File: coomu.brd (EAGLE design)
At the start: 25 x 12.1 mm, 23 parts

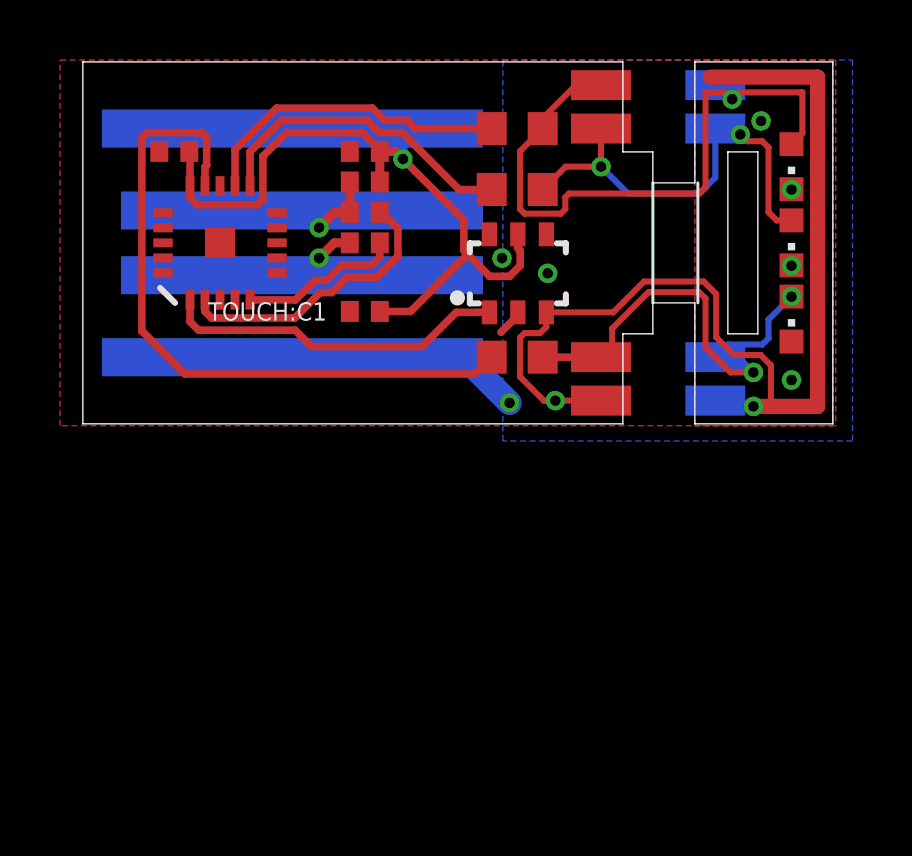
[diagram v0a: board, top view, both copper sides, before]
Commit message: Bob pointed out that LEDs that fire sideways exist. So much simpler.
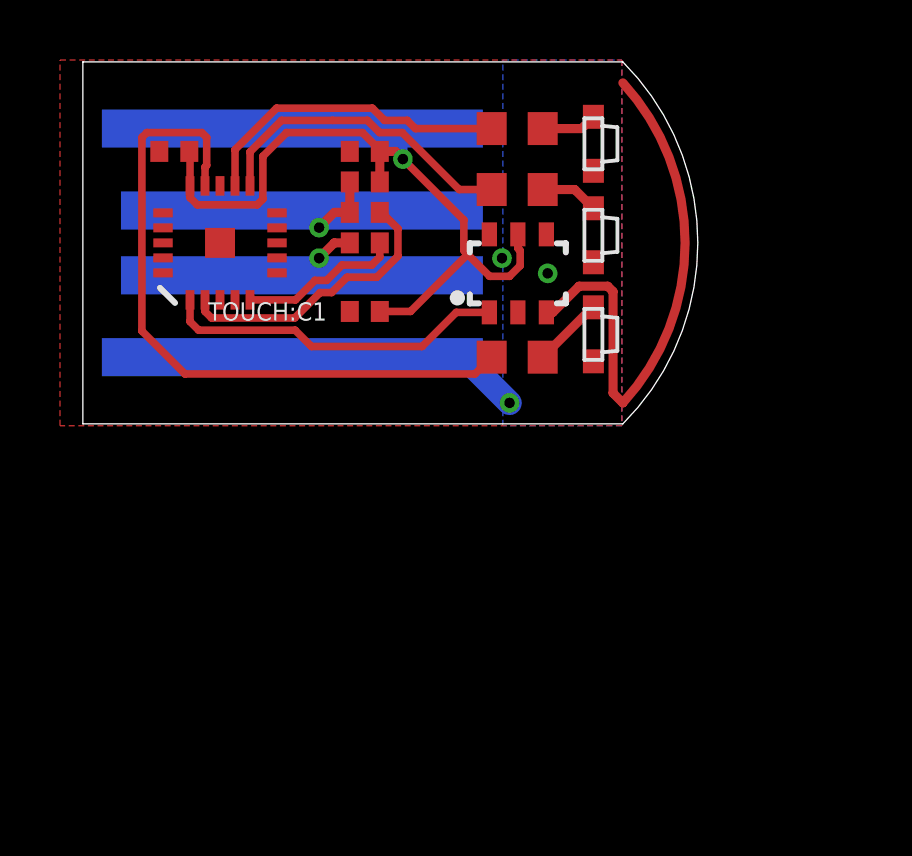
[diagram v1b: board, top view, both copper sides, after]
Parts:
- removed LEDS:U$1, LEDS:U$2, LEDS:U$3, LEDS:U$4, LEDS:U$5, LEDS:U$6, TOUCH:U$2, TOUCH:U$3: PAD, coomu:PAD-1.0-2.0
- LEDS:BLUE: value LED_灯_蓝_Iv=11.5-28.5_λd=465-475 -> LED-SIDEFIRE0603; device JLCPCB.Optocouplers & LEDs & Infrared.basic:LED_0603 -> coomu:LED-0603-SIDEFIRE
- LEDS:GREEN: value LED_灯_绿_Iv=112-285_λd=520-535 -> LED-SIDEFIRE0603; device JLCPCB.Optocouplers & LEDs & Infrared.basic:LED_0603 -> coomu:LED-0603-SIDEFIRE
- LEDS:RED: value LED_灯_红_Iv=100-120_λd=615-630 -> LED-SIDEFIRE0603; device JLCPCB.Optocouplers & LEDs & Infrared.basic:LED_0603 -> coomu:LED-0603-SIDEFIRE
- moved LEDS:BLUE 6.65 mm to (17.0, 3.30), turned to 270 degrees
- moved LEDS:RED 6.62 mm to (17.0, -3.05), turned to 270 degrees
- moved LEDS:GREEN 6.61 mm to (17.0, 0.25), turned to 270 degrees
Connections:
- net GND: now also LEDS:BLUE.P$1, LEDS:GREEN.P$1, LEDS:RED.P$1; no longer LEDS:BLUE.C, LEDS:GREEN.C, LEDS:RED.C
- net LEDS:N$1: now also LEDS:RED.P$2; no longer LEDS:RED.A, LEDS:U$1.P$1, LEDS:U$2.P$1
- net LEDS:N$2: now also LEDS:GREEN.P$2; no longer LEDS:GREEN.A, LEDS:U$3.P$1, LEDS:U$4.P$1
- net LEDS:N$3: now also LEDS:BLUE.P$2; no longer LEDS:BLUE.A, LEDS:U$5.P$1, LEDS:U$6.P$1
- net TOUCH:SENSE: no longer TOUCH:U$2.P$1, TOUCH:U$3.P$1
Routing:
- net LEDS:N$3: track 21.9 -> 1.85 mm, vias 1 -> 0
- net TOUCH:SENSE: track 35.2 -> 17.2 mm, vias 2 -> 0
- net LEDS:N$1: track 15.5 -> 2.38 mm, vias 2 -> 0
- net LEDS:N$2: track 14.6 -> 1.95 mm, vias 2 -> 0
- net GND: track 8.77 -> 7.87 mm, vias 7 -> 3
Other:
- board size 25 x 12.1 mm -> 20.5 x 12.1 mm

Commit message: Made it shorter so it fits snugger in a port
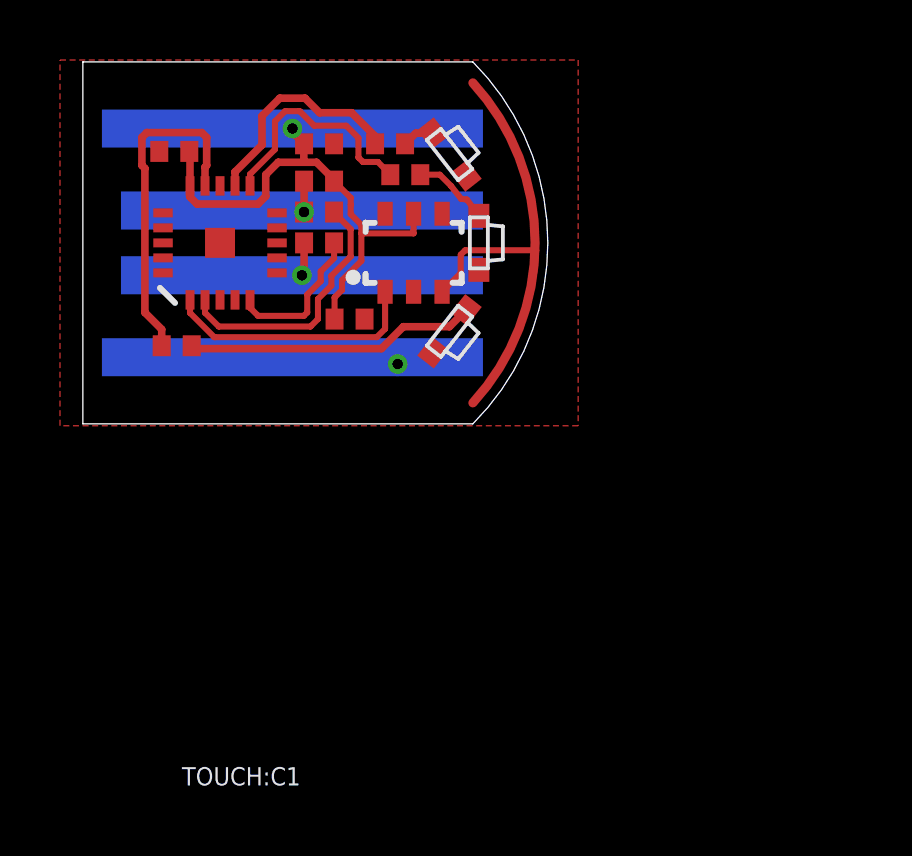
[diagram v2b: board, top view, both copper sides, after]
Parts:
- LEDS:R1: device JLCPCB.Resistors.basic:RESISTOR_0603 -> JLCPCB.Resistors.basic:RESISTOR_0402
- LEDS:R2, LEDS:R3: value 82Ω -> 100Ω; device JLCPCB.Resistors.basic:RESISTOR_0603 -> JLCPCB.Resistors.basic:RESISTOR_0402
- moved LEDS:R1 11.4 mm to (3.13, -3.43)
- moved LEDS:BLUE 4.81 mm to (12.2, 2.95), turned to 308 degrees
- moved LEDS:RED 4.80 mm to (12.2, -2.95), turned to 232 degrees
- moved LEDS:R3 4.27 mm to (10.2, 3.30)
- moved LEDS:GREEN 3.83 mm to (13.2, 0.00)
- moved LEDS:R2 3.76 mm to (10.7, 2.27)
- moved TOUCH:U$1 3.54 mm to (11.0, -0.33)
- moved MCU:C2 1.55 mm to (7.87, 3.30), turned to 0 degrees
- moved MCU:R3 1.52 mm to (7.87, 2.06)
- moved MCU:R2 1.52 mm to (7.87, 1.03)
- moved MCU:R1 1.52 mm to (7.87, 0.00)
- moved TOUCH:C1 0.57 mm to (8.89, -2.54), turned to 0 degrees
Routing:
- net RED: track 22.9 -> 11.1 mm
- net 5V: track 27.8 -> 16.8 mm
- net LEDS:N$1: track 2.38 -> 9.72 mm
- net GND: track 7.87 -> 3.60 mm, vias 3 -> 1
- net BLUE: track 10.6 -> 7.50 mm
- net TOUCH:SENSE: track 17.2 -> 20.2 mm
- net Q: track 11.5 -> 8.62 mm
- net GREEN: track 10.6 -> 7.74 mm
- net USB_D-: track 3.06 -> 1.12 mm
- net LEDS:N$3: track 1.85 -> 1.07 mm
- net MCU:PB3: track 9.51 -> 8.74 mm
- net LEDS:N$2: track 1.95 -> 2.60 mm
- net USB_D+: track 2.04 -> 2.56 mm
- removed copper zone on layer 16, net GND
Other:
- board size 20.5 x 12.1 mm -> 15.5 x 12.1 mm
